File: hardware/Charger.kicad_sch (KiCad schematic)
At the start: 0 parts

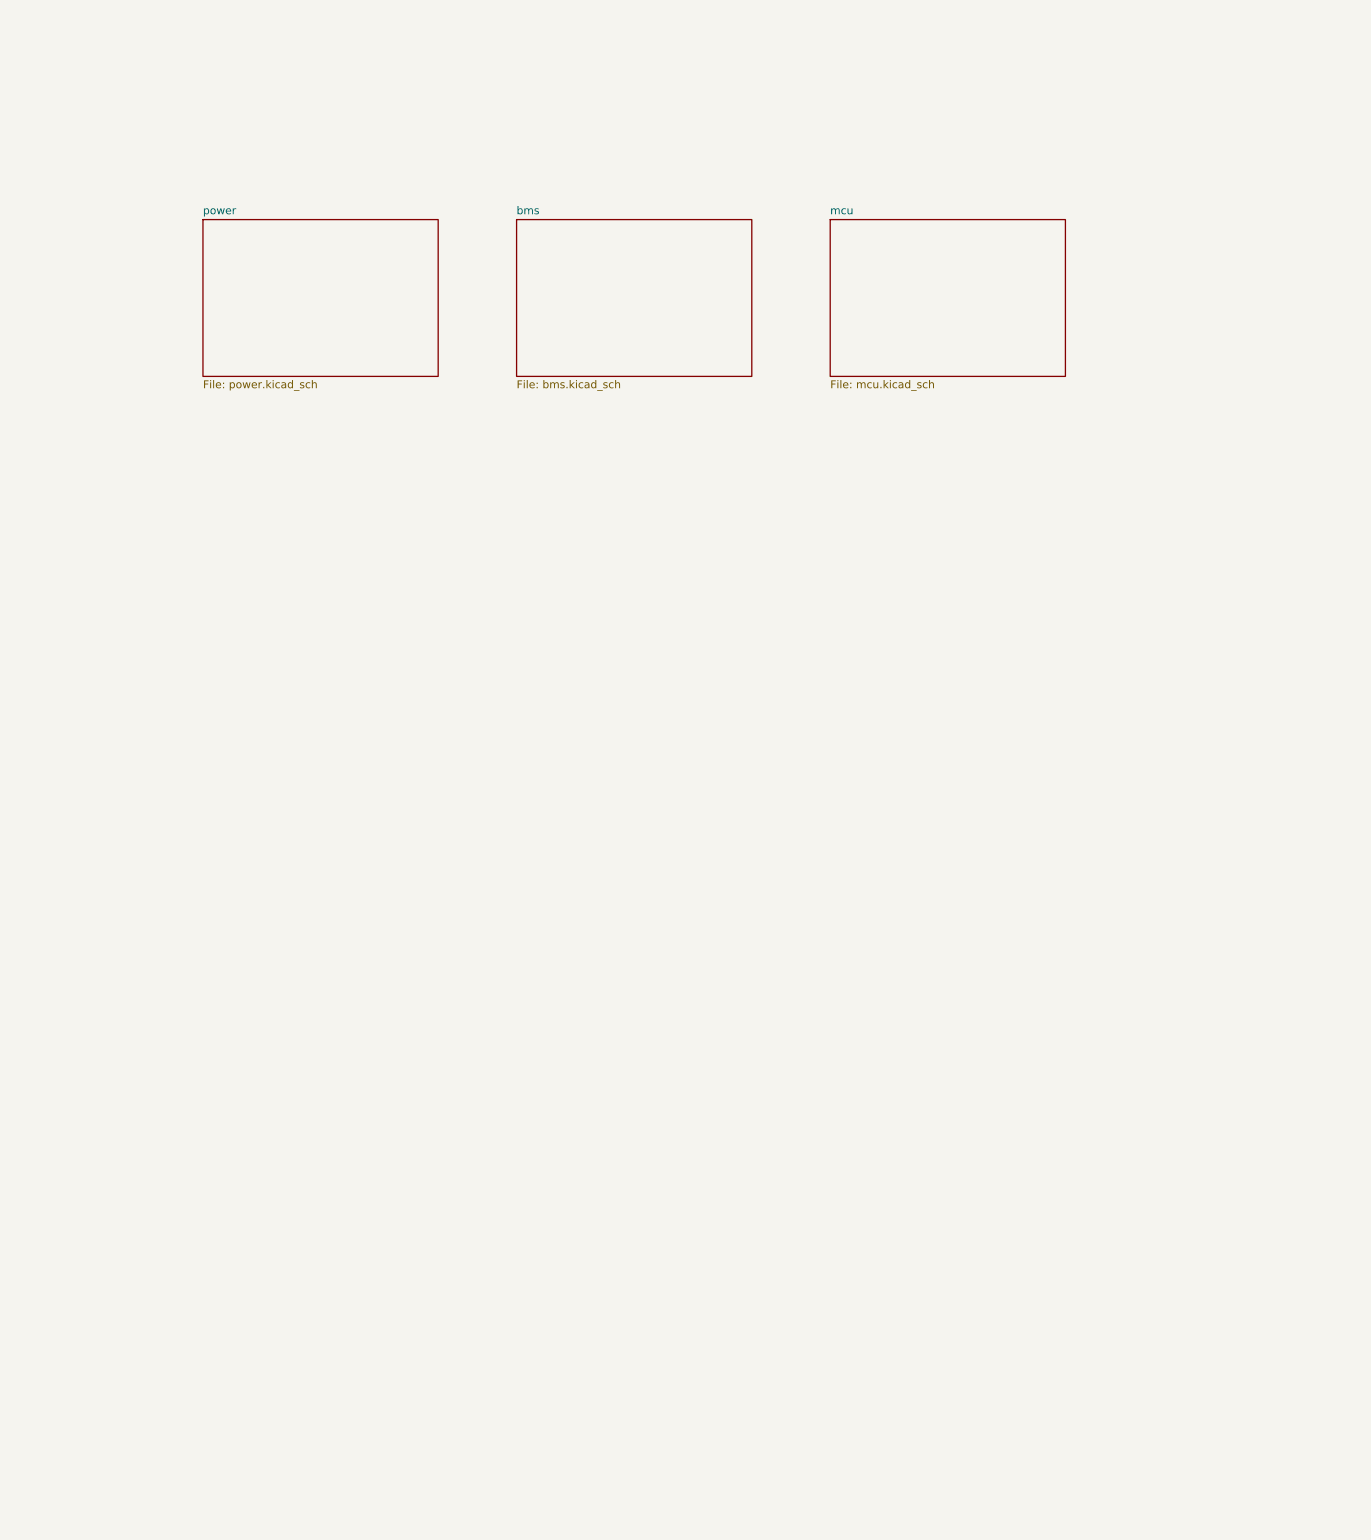
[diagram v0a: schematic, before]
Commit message: feat(charger): PCB start, hierarchical schematic rework, sourced lib parts
Restructure schematic from bms/mcu/power sheets into main + cell
hierarchy, update root sheet and project settings, add first
Charger.kicad_pcb layout, and land the sourced local library additions
(symbols, 92 footprints, 96 3D models) backing the reworked design.

Co-Authored-By: Claude Fable 5 <noreply@anthropic.com>
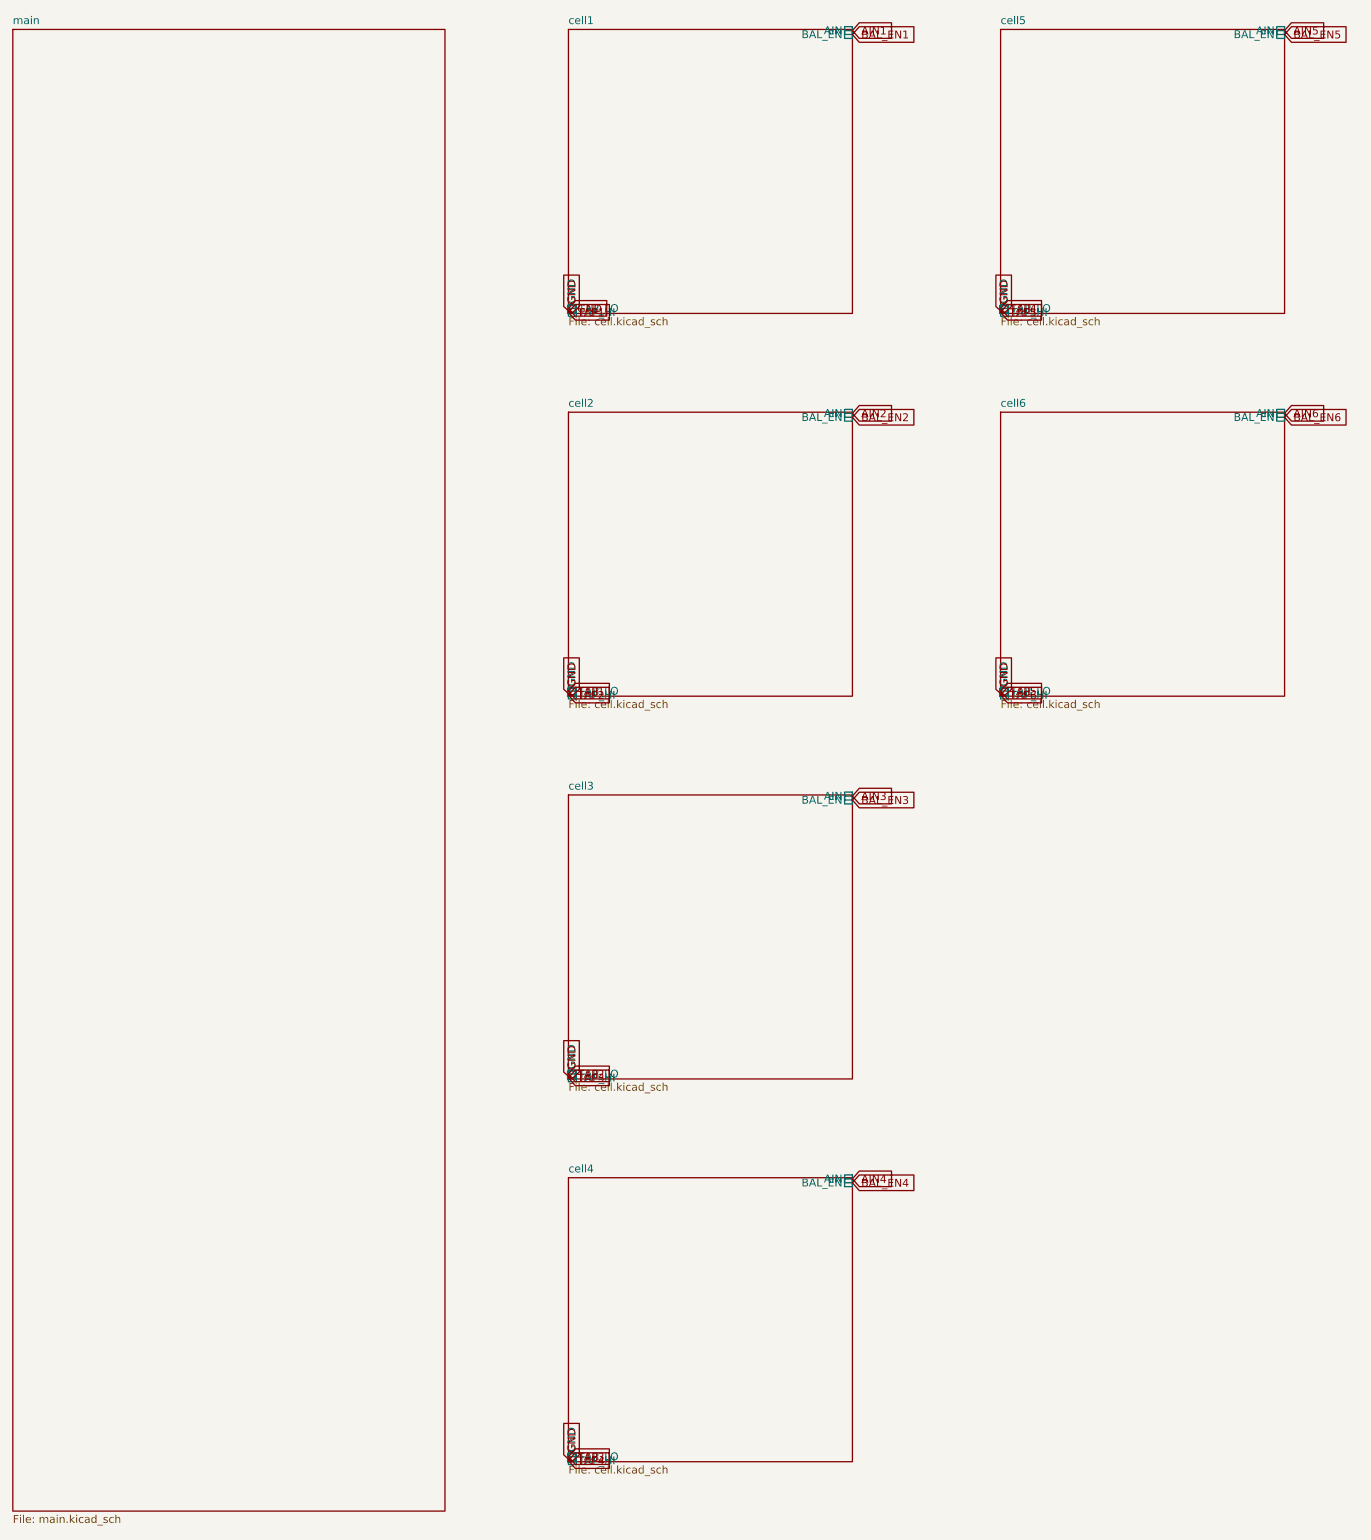
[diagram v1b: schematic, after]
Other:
- removed sheet bms
- removed sheet mcu
- removed sheet power
- added sheet cell1 (cell.kicad_sch)
- added sheet cell2 (cell.kicad_sch)
- added sheet cell3 (cell.kicad_sch)
- added sheet cell4 (cell.kicad_sch)
- added sheet cell5 (cell.kicad_sch)
- added sheet cell6 (cell.kicad_sch)
- added sheet main (main.kicad_sch)
